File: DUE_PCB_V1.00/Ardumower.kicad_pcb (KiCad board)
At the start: 2 copper layers, 169.4 x 95.6 mm, 72 parts, among them J1 9V IN, J10 Sonar_R, J11 Sonar_C, J12 Sonar_L, J13 P_Right, J14 Buzzer, J15 Button, J16 US1, J17 US2, J18 US3, J19 P_Left, J2 I2C0_1, J20 Remote, J21 PCB_2, J22 Ser0, J23 Ser1, J24 Ser2, J25 5V IN, J26 Cutter, J27 MotorR, J28 MotorL, J29 3.3V IN, J3 I2C0_2, J30 I2C1_2, J31 Ser3, J32 24V In, J33 ReserveD8, J34 ReserveD9, J35 ReserveD49, J36 ReserveA10, J4 I2C1_1, J5 Bumper, J6 Drop_Left, J7 Drop_Right, J8 Tilt, J9 Rain, U1 MC33926, U2 MC33926

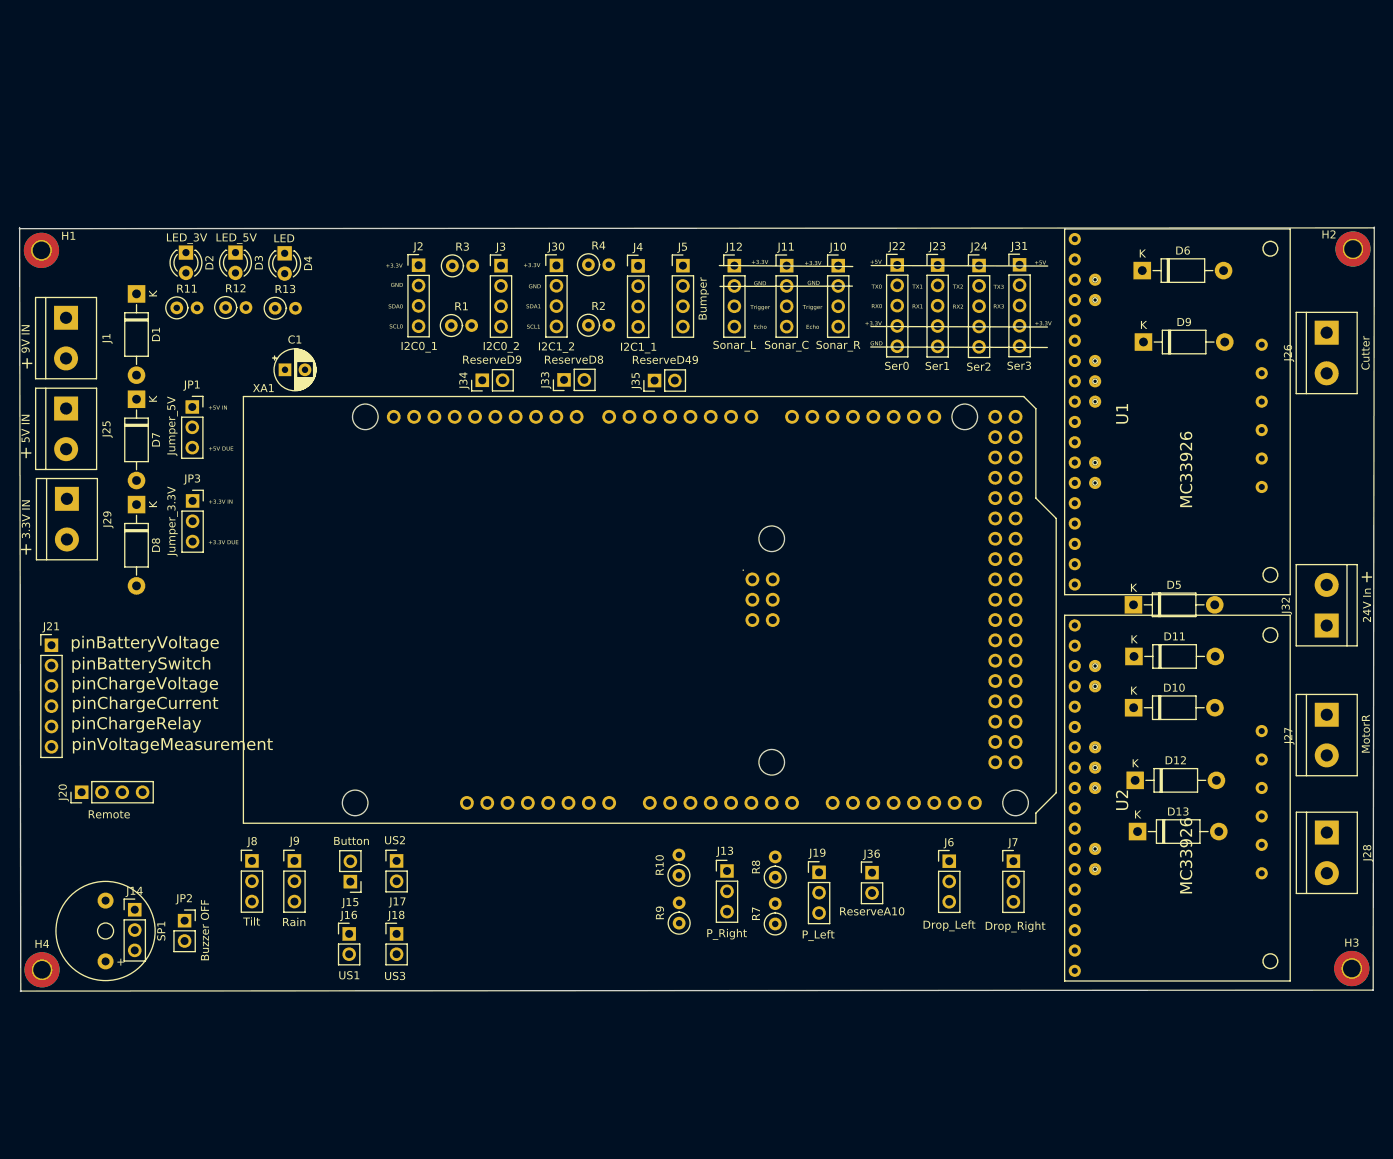
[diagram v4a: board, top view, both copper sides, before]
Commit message: Add PCB Pin Description
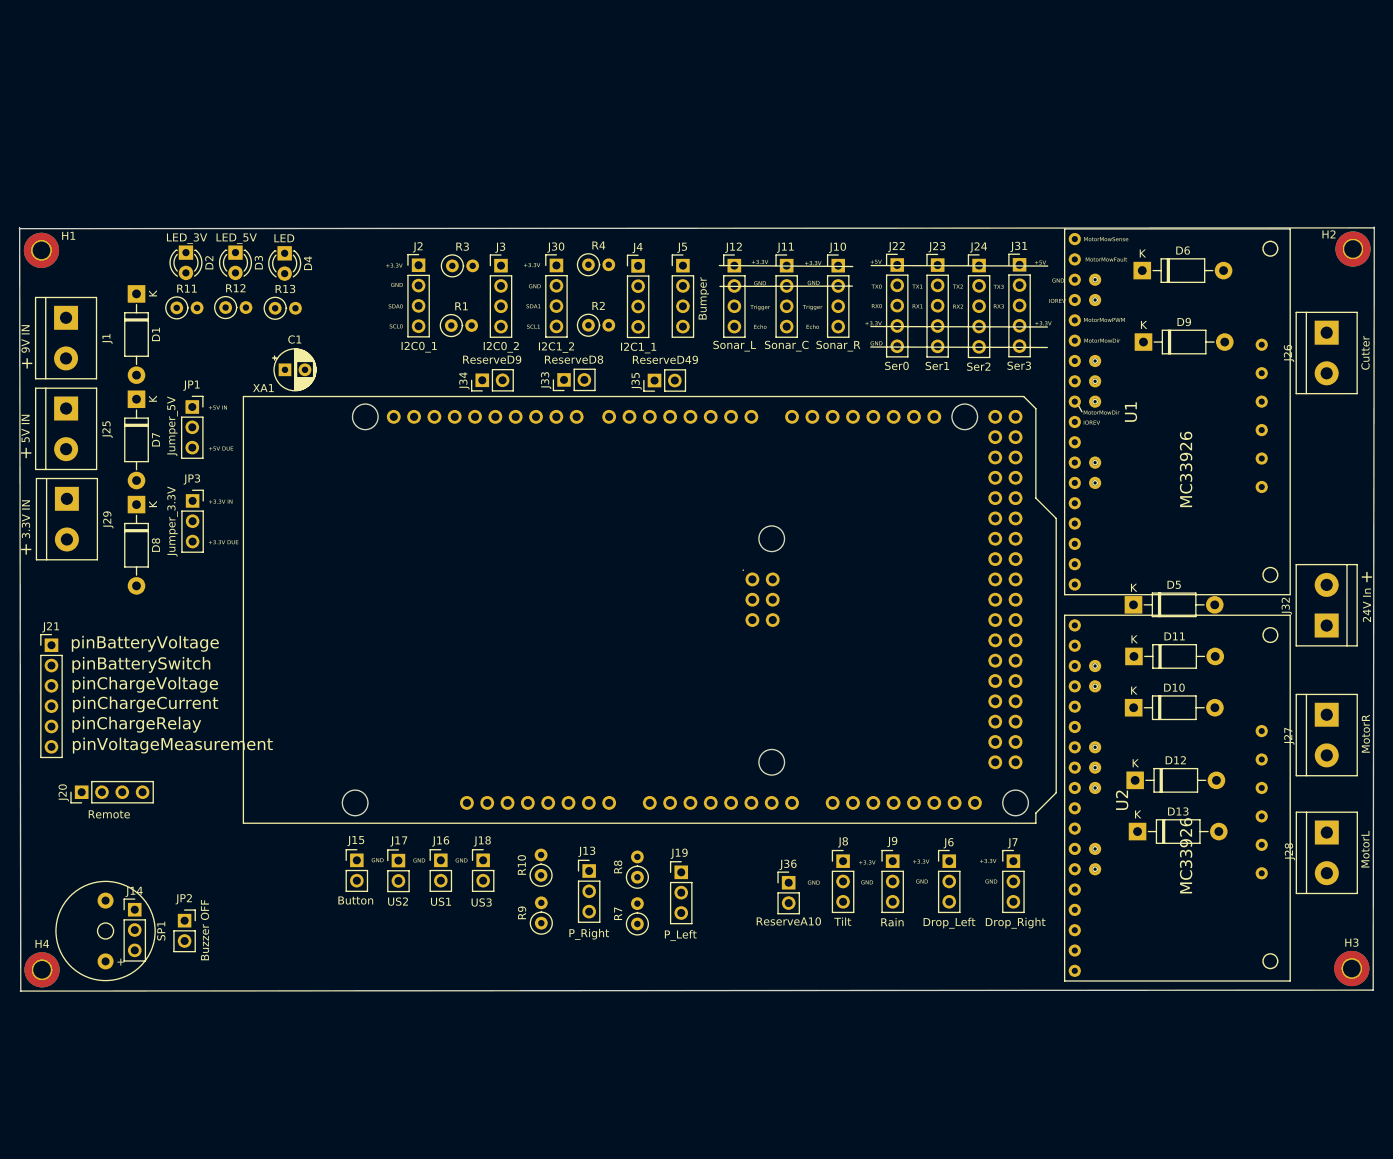
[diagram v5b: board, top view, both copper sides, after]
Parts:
- moved J9 74.8 mm to (148.2, 114.8)
- moved J8 73.9 mm to (142.0, 114.8)
- moved J13 17.2 mm to (110.3, 116.0)
- moved R7 17.2 mm to (116.3, 122.6)
- moved R8 17.2 mm to (116.3, 116.8)
- moved J19 17.2 mm to (121.8, 116.2)
- moved R10 17.2 mm to (104.3, 116.6)
- moved R9 17.2 mm to (104.3, 122.5)
- moved J16 14.7 mm to (91.7, 114.7)
- moved J18 14.2 mm to (97.0, 114.7)
- moved J36 10.5 mm to (135.2, 117.5)
- moved J15 2.78 mm to (81.2, 114.7), turned to 0 degrees
- moved J17 0.23 mm to (86.4, 114.7)
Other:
- net class 24v added: clearance 0.254, trace_width 0.5, via_dia 0.889, via_drill 0.635
- net class Default: clearance 0.2 -> 0.254; trace_width 0.25 -> 0.254; via_dia 0.8 -> 0.889; via_drill 0.4 -> 0.635
- net class GND added: clearance 0.254, trace_width 0.5, via_dia 0.889, via_drill 0.635
- net class Power added: clearance 0.254, trace_width 0.354, via_dia 0.889, via_drill 0.635
- rule trace_clearance: 0.2 -> 0.254
- rule trace_min: 0.2 -> 0.254
- rule via_min_drill: 0.3 -> 0.508
- rule via_min_size: 0.4 -> 0.889
- board text added: "IOREV"
- board text added: "MotorMowDir"
- board text added: "MotorMowFault"
- board text added: "MotorMowPWM"
- board text added: "MotorMowSense"

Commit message: Add PCB Pin Description
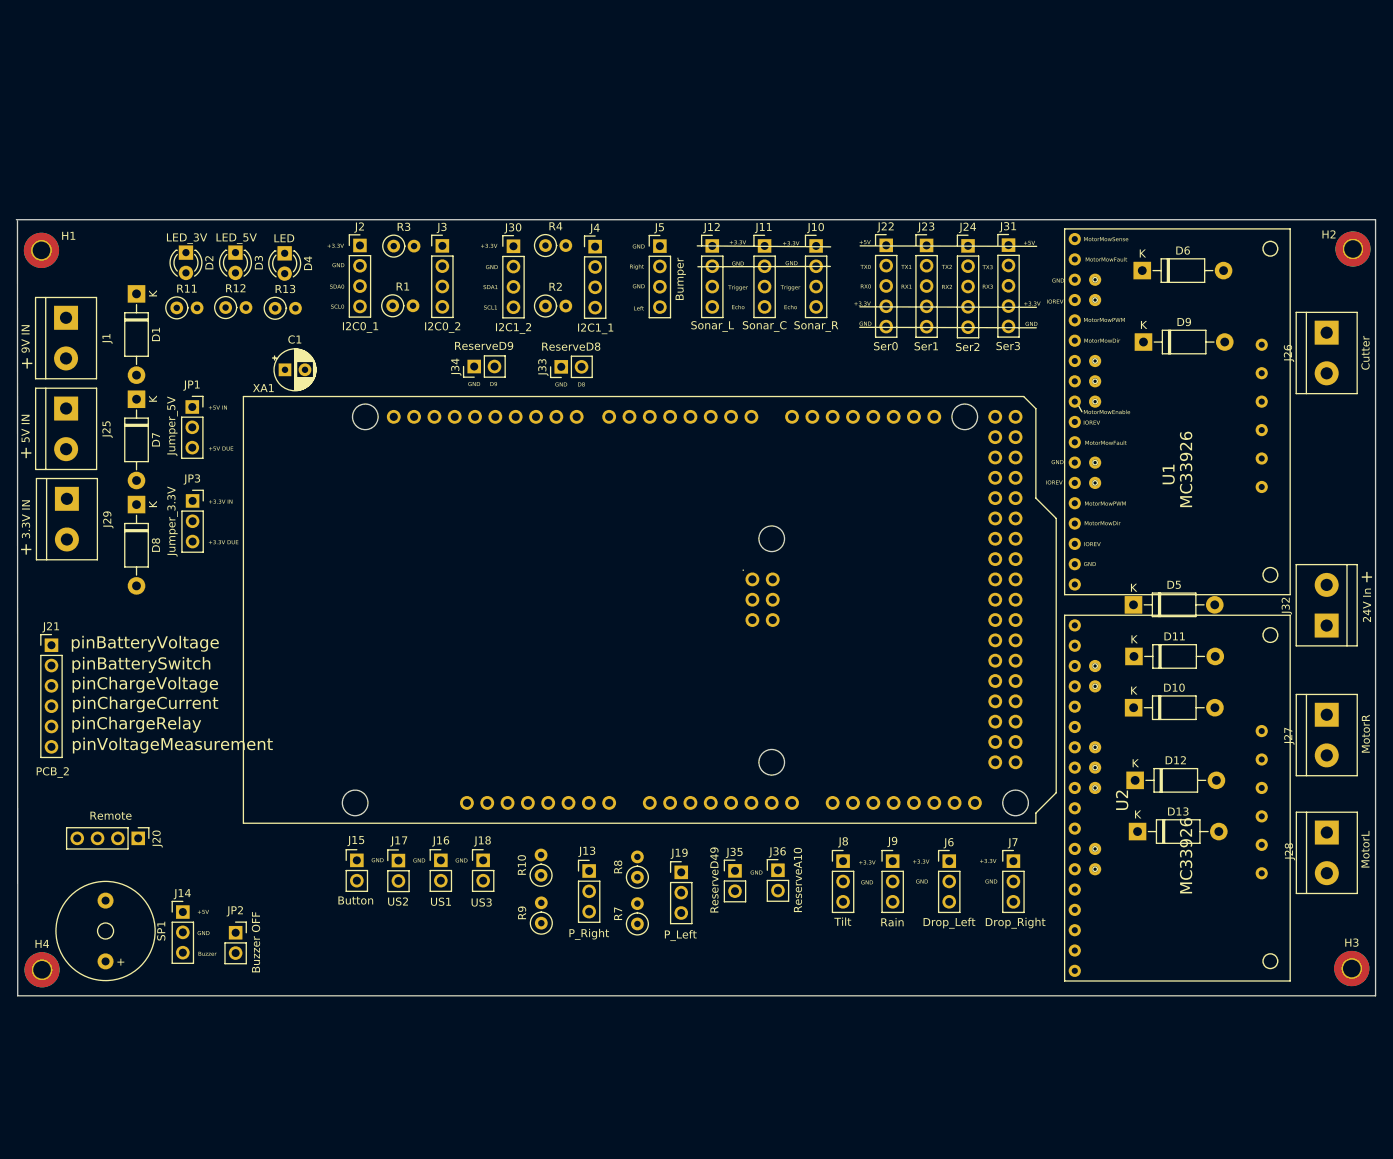
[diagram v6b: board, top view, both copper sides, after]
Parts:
- moved J35 62.1 mm to (128.5, 116.0), turned to 0 degrees
- moved J20 9.13 mm to (53.9, 111.9), turned to 270 degrees
- moved R1 7.73 mm to (85.7, 45.4)
- moved R3 7.73 mm to (85.8, 37.9)
- moved J2 7.73 mm to (81.6, 37.8)
- moved J3 7.73 mm to (91.9, 37.9)
- moved JP2 6.56 mm to (66.1, 123.7)
- moved J14 6.02 mm to (59.5, 121.2)
- moved J4 5.88 mm to (111.0, 38.0)
- moved J30 5.88 mm to (100.8, 37.9)
- moved R2 5.88 mm to (104.8, 45.4)
- moved R4 5.88 mm to (104.8, 37.8)
- moved J5 3.77 mm to (119.1, 37.9)
- moved J10 3.70 mm to (138.6, 37.9)
- moved J11 3.70 mm to (132.2, 37.9)
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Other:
- board size 169.4 x 95.6 mm -> 169.9 x 97 mm
- board text added: "Buzzer"
- board text added: "D8"
- board text added: "D9"
- board text added: "Left"
- board text added: "MotorMowEnable"
- board text added: "Right"

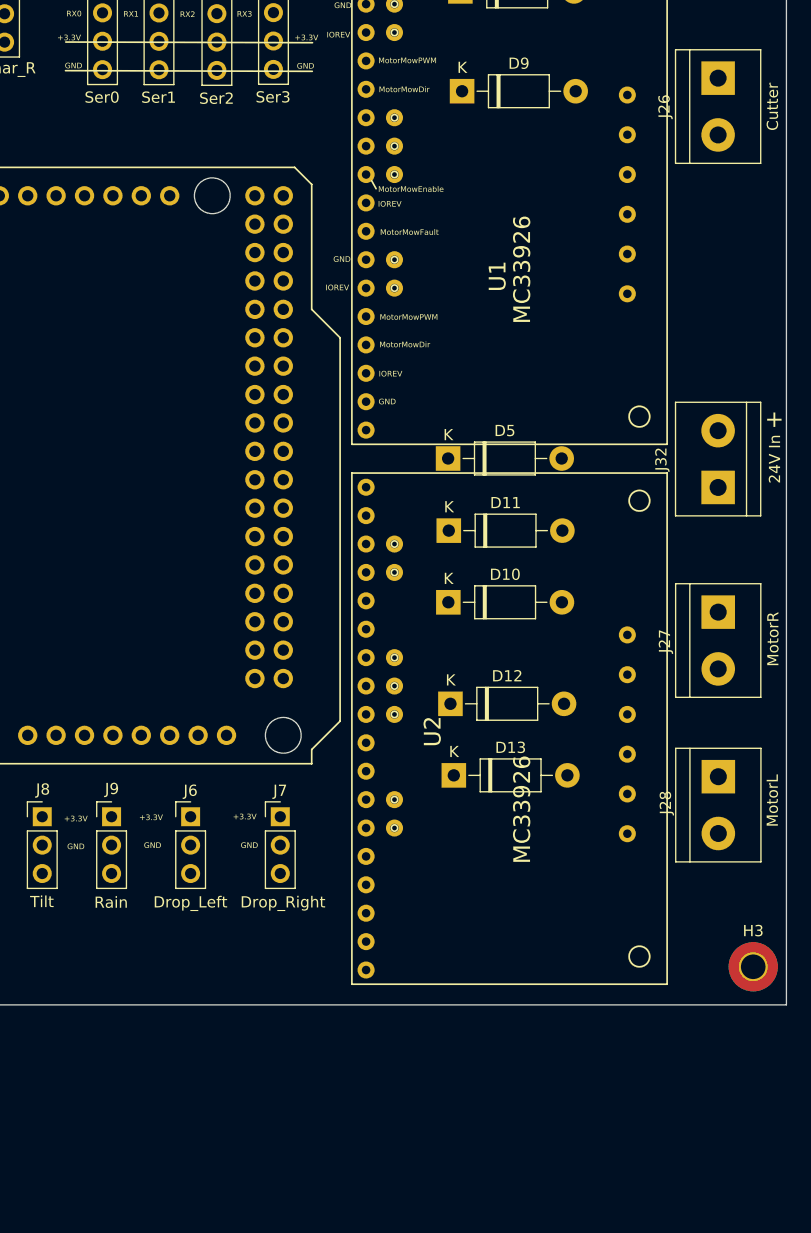
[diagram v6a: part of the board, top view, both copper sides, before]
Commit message: Add Voltage Divider to ODO
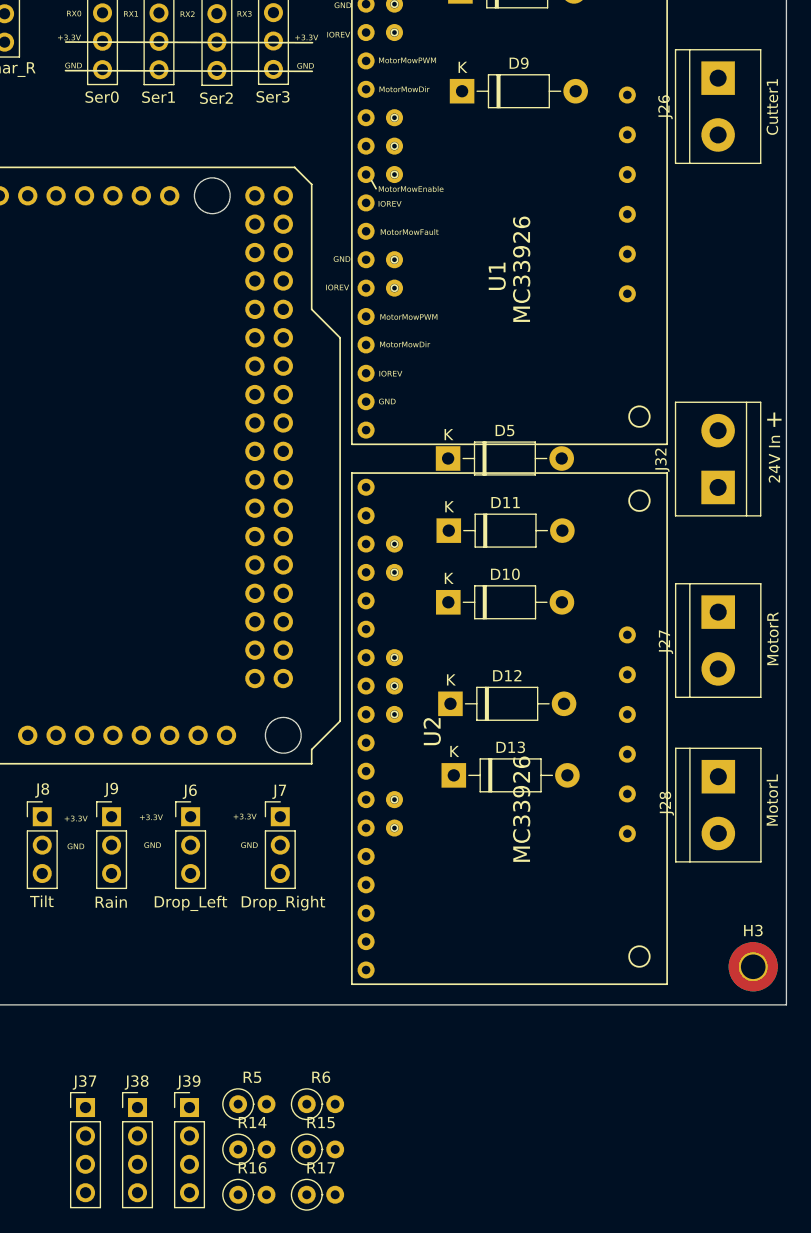
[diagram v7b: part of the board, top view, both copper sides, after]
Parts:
- added J37: RPM_Mow, Connector_PinHeader_2.54mm:PinHeader_1x04_P2.54mm_Vertical, F.Cu at (145.9, 140.8)
- added J38: ODO_Left, Connector_PinHeader_2.54mm:PinHeader_1x04_P2.54mm_Vertical, F.Cu at (150.5, 140.8)
- added J39: ODO_Right, Connector_PinHeader_2.54mm:PinHeader_1x04_P2.54mm_Vertical, F.Cu at (155.2, 140.8)
- added R14: 1KO, Resistor_THT:R_Axial_DIN0207_L6.3mm_D2.5mm_P2.54mm_Vertical, F.Cu at (159.5, 144.6)
- added R15: 1,5KO, Resistor_THT:R_Axial_DIN0207_L6.3mm_D2.5mm_P2.54mm_Vertical, F.Cu at (165.7, 144.6)
- added R16: 1,5KO, Resistor_THT:R_Axial_DIN0207_L6.3mm_D2.5mm_P2.54mm_Vertical, F.Cu at (159.5, 148.6)
- added R17: 1,5KO, Resistor_THT:R_Axial_DIN0207_L6.3mm_D2.5mm_P2.54mm_Vertical, F.Cu at (165.7, 148.6)
- added R5: 1KO, Resistor_THT:R_Axial_DIN0207_L6.3mm_D2.5mm_P2.54mm_Vertical, F.Cu at (159.5, 140.5)
- added R6: 1KO, Resistor_THT:R_Axial_DIN0207_L6.3mm_D2.5mm_P2.54mm_Vertical, F.Cu at (165.7, 140.5)
- J26: value Cutter -> Cutter1
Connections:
- XA1 pad A11: (no net) -> pinMotorMowRpm
- XA1 pad CANR: (no net) -> pinOdometryRight
- XA1 pad DAC0: (no net) -> pinOdometryLeft
